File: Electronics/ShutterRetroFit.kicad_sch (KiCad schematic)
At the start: 20 parts, among them J1 AMPHENOL_12402012E212A, J2 AS5600, J3 Motor Terminals, Q1 SiSS52DN-T1-GE3, Q2 SiSS52DN-T1-GE3, Q3 SiSS52DN-T1-GE3, Q4 SiSS52DN-T1-GE3, U1 ESP32-WROOM-32, U2 CP2102N-Axx-xQFN28, U3 MIC4606-2YTS-TR, U4 AMS1117-3.3 (Potentially swap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, U5 LM2576S-ADJ

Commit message: Bulk sync with various changes made over the last year
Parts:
- removed F1, F2: Fuse, symbol Device:Fuse
- removed J2: AS5600, symbol Connector:Conn_01x04_Socket
- removed J3: Motor Terminals, symbol Connector:Conn_01x02_Pin
- removed Q1, Q2, Q3, Q4: SiSS52DN-T1-GE3, SISS94DNT1GE3, symbol CustomLibrary:SiSS52DN-T1-GE3
- removed R1: R_Shunt, symbol Device:R_Shunt
- removed RV1: R_Potentiometer_Trim, symbol Device:R_Potentiometer_Trim
- removed TH1, TH2, TH3, TH4: Thermistor, symbol Device:Thermistor
- removed U3: MIC4606-2YTS-TR, TSSOP16_TS_MCH_MIS, symbol CustomLibrary:MIC4606-2YTS-TR
- removed U4: AMS1117-3.3 (Potentially swap for a better LDO), Package_TO_SOT_SMD:SOT-223-3_TabPin2, symbol Regulator_Linear:AMS1117-3.3
- removed U5: LM2576S-ADJ, Package_TO_SOT_SMD:TO-263-5_TabPin3, symbol Regulator_Switching:LM2576S-ADJ
- added C1, C3, C5, C6, C7, C8: 0.1uF, Capacitor_SMD:C_0603_1608Metric_Pad1.08x0.95mm_HandSolder, symbol Device:C
- added C2: 1uF, Capacitor_SMD:C_0603_1608Metric_Pad1.08x0.95mm_HandSolder, symbol Device:C
- added C4: 22uF, Capacitor_SMD:C_0603_1608Metric_Pad1.08x0.95mm_HandSolder, symbol Device:C
- added H1, H2, H3, H4: MountingHole_Pad, MountingHole:MountingHole_3.2mm_M3_DIN965_Pad, symbol Mechanical:MountingHole_Pad
- added J2: AS5600, Connector_JST:JST_XH_B6B-XH-A_1x06_P2.50mm_Vertical, symbol Connector:Conn_01x06_Socket
- added J3: PWR_IN+, CustomLibrary:CONN_726386-2_TEC, symbol Connector:Conn_01x01_Pin
- added J4: EXP, Connector_PinHeader_2.54mm:PinHeader_1x06_P2.54mm_Vertical, symbol Connector:Conn_01x06_Pin
- added J5: CONTROL, Connector_JST:JST_XH_B6B-XH-A_1x06_P2.50mm_Vertical, symbol Connector:Conn_01x06_Socket
- added J6: PWR_IN-, CustomLibrary:CONN_726386-2_TEC, symbol Connector:Conn_01x01_Pin
- added R1, R2: 5k1, Resistor_SMD:R_0603_1608Metric_Pad0.98x0.95mm_HandSolder, symbol Device:R
- added R3, R4: 1k, Resistor_SMD:R_0603_1608Metric_Pad0.98x0.95mm_HandSolder, symbol Device:R
- added SW1: RESET, symbol Switch:SW_SPST
- added SW2: BOOT, symbol Switch:SW_SPST
- added TP1: RX, TestPoint:TestPoint_Pad_D1.0mm, symbol Connector:TestPoint
- added TP2: TX, TestPoint:TestPoint_Pad_D1.0mm, symbol Connector:TestPoint
- added TP3: IO0, TestPoint:TestPoint_Pad_D1.0mm, symbol Connector:TestPoint
- added TP4: EN, TestPoint:TestPoint_Pad_D1.0mm, symbol Connector:TestPoint
- U1: renamed from U2; value CP2102N-Axx-xQFN28 -> CP2102-Axx-xQFN28
- renumbered U1 to U2
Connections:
- net GND: now reaches J1.A1_B12 (GND)
- net GND: now also J1.B1_A12 (GND__1), J1.SH1 (SHIELD), J1.SH2 (SHIELD__1), J1.SH3 (SHIELD__2), J1.SH4 (SHIELD__3), U1.29 (GND), U1.3 (GND), U2.1 (GND), U2.15 (GND), U2.38 (GND), U2.39 (GND), C1.2, C2.2, C3.2, C4.2, C5.2, C6.2, C7.2, C8.2, H1.1, H2.1, H3.1, H4.1, J2.1 (Pin_1), J2.2 (Pin_2), J4.1 (Pin_1), J5.1 (Pin_1), J6.1 (Pin_1), R1.2, R2.2, SW1.2 (B), SW2.2 (B)
- net USB_{VBUS}: now reaches J1.A4_B9 (VBUS)
- net USB_{VBUS}: now also J1.B4_A9 (VBUS__1), U1.7 (VREGIN), U1.8 (VBUS), C2.1, C3.1
- net at J1.A5 (CC1_A): now also R1.1
- net DATA+: now reaches J1.A6 (D+_A)
- net DATA+: now also J1.B6 (D+_B), U1.4 (D+)
- net DATA-: now reaches J1.A7 (D-_A)
- net DATA-: now also J1.B7 (D-_B), U1.5 (D-)
- net at J1.B5 (CC1_B): now also R2.1
- net UART_{RX}: now reaches U1.25 (RXD)
- net UART_{RX}: now also U2.35 (TXD0/IO1), TP1.1
- net UART_{TX}: now reaches U1.26 (TXD)
- net UART_{TX}: now also U2.34 (RXD0/IO3), TP2.1
- net at U1.6 (VDD): now also C1.1
- net EXP_{02}: now reaches U2.10 (IO25)
- net EXP_{02}: now also J4.3 (Pin_3)
- net EXP_{01}: now reaches U2.11 (IO26)
- net EXP_{01}: now also J4.2 (Pin_2)
- net BTN_{UP}: now reaches U2.12 (IO27)
- net BTN_{UP}: now also C7.1, J5.3 (Pin_3), R3.1
- net H_{DRIVER_LEFT_EN}: now reaches U2.13 (IO14)
- net H_{DRIVER_LEFT_CONTROL}: now reaches U2.14 (IO12)
- net H_{DRIVER_RIGHT_EN}: now reaches U2.16 (IO13)
- net MCU_{VIN}: now reaches U2.2 (VDD)
- net MCU_{VIN}: now also C4.1
- net H_{DRIVER_RIGHT_CONTROL}: now reaches U2.23 (IO15)
- net IO0: now reaches U2.25 (IO0)
- net IO0: now also C5.1, SW1.1 (A), TP3.1
- net M_{SENSE}: now reaches U2.27 (IO16)
- net D_{POWER}: now reaches U2.28 (IO17)
- net D_{POWER}: now also J5.6 (Pin_6)
- net EN: now reaches U2.3 (EN)
- net EN: now also C6.1, SW2.1 (A), TP4.1
- net D_{STATUS}: now reaches U2.30 (IO18)
- net D_{STATUS}: now also J5.5 (Pin_5)
- net D_{ERROR}: now reaches U2.31 (IO19)
- net D_{ERROR}: now also J5.4 (Pin_4)
- net AS5600_{SDA}: now reaches U2.33 (IO21)
- net AS5600_{SDA}: now also J2.4 (Pin_4)
- net AS5600_{SCL}: now reaches U2.36 (IO22)
- net AS5600_{SCL}: now also J2.5 (Pin_5)
- net BTN_{DOWN}: now reaches U2.8 (IO32)
- net BTN_{DOWN}: now also C8.1, J5.2 (Pin_2), R4.1
- new net +12V: J3.1 (Pin_1)
- new net +12v_{EXP}: J4.6 (Pin_6)
- new net +3V3: R3.2, R4.2
- new net +3v3_{EXP}: J2.6 (Pin_6), J4.4 (Pin_4)
- new net +5v_{EXP}: J4.5 (Pin_5)
- no-connect marks 0 -> 1
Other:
- added sheet Motor (motor_sch.kicad_sch)
- added sheet Power Rails (PowerRails.kicad_sch)
- note added: "3.3v at Gate 12v at Source ~0v at Drain V_{gs} = 3.3v - 12v = ~ -8.7v V_{ds} = ~ -12v"
- note added: "Button pannel buttons should be pulling to ground"
- note added: "Do we want D+ and D- TPs?"
- note added: "V_{gs} > ~2v starts to conduct current To get optimal Rds_{on} then V_{gs} >= 6v Since these are low side mosfet, check what voltage they'd be recieving at the drain Theoretically this is fine as when conducting V_{gs} will be 3.3v and when not conducting stil 3.3v"
- company: (none) -> TowKnee
- title: (none) -> Shutter Motor Retro Fit
- moved on the sheet: J1, U1, U2

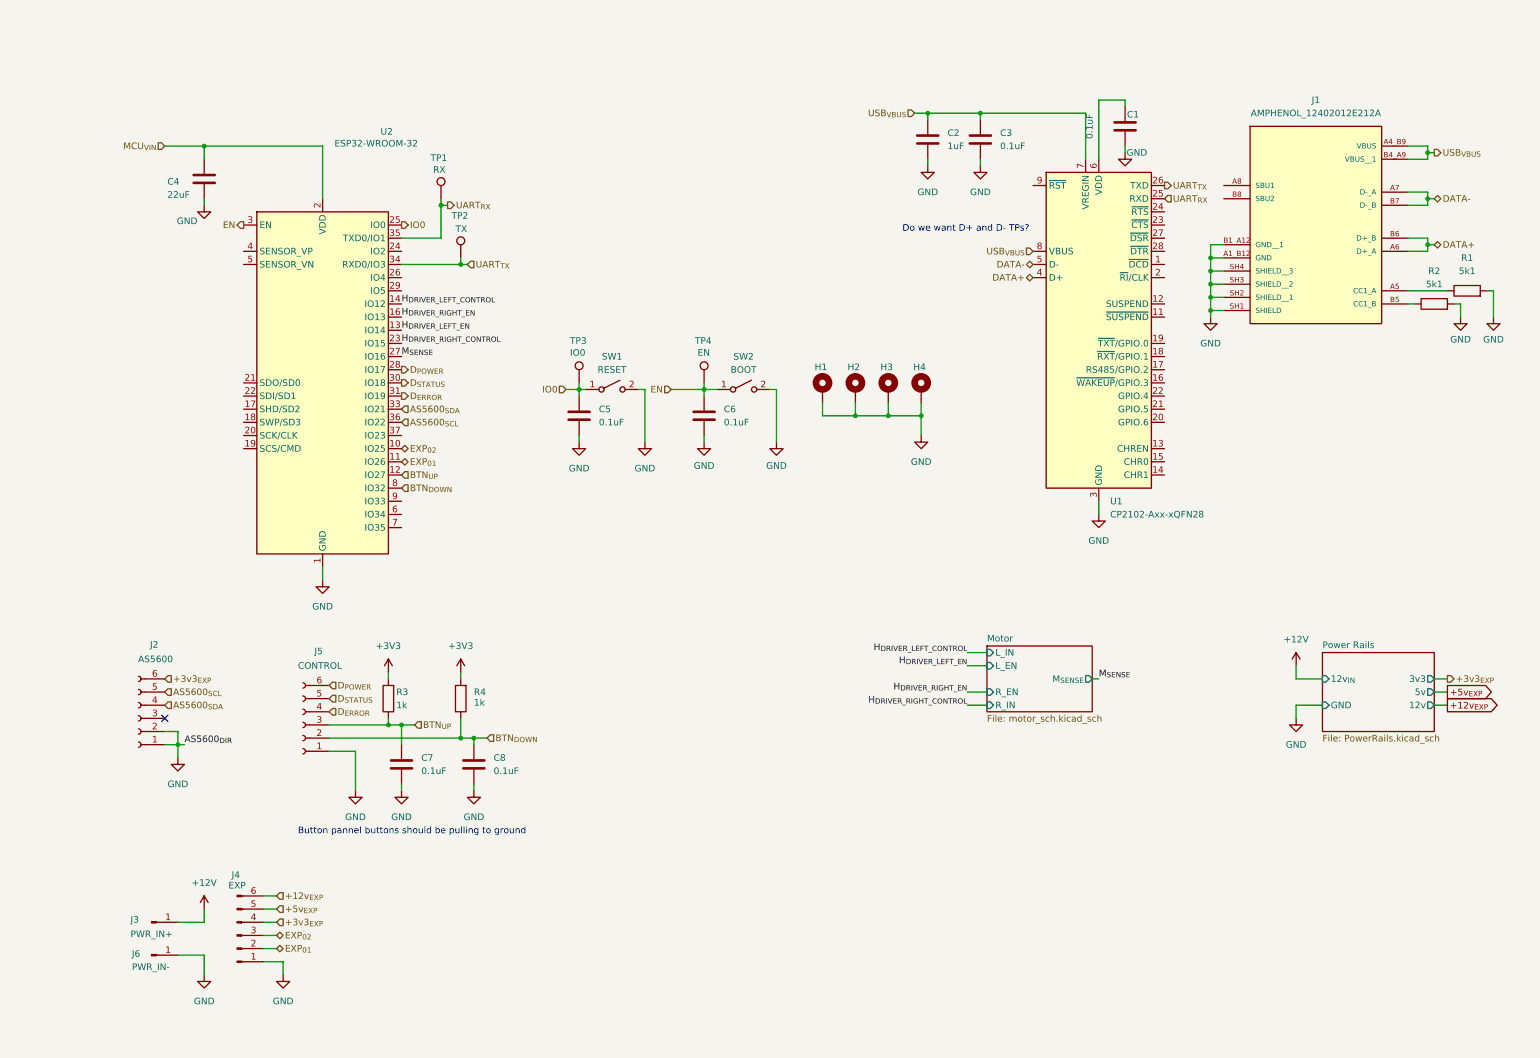
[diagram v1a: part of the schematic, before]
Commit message: Clean up schematic to be neater and repurposed AS5600 to be generic accessory connector
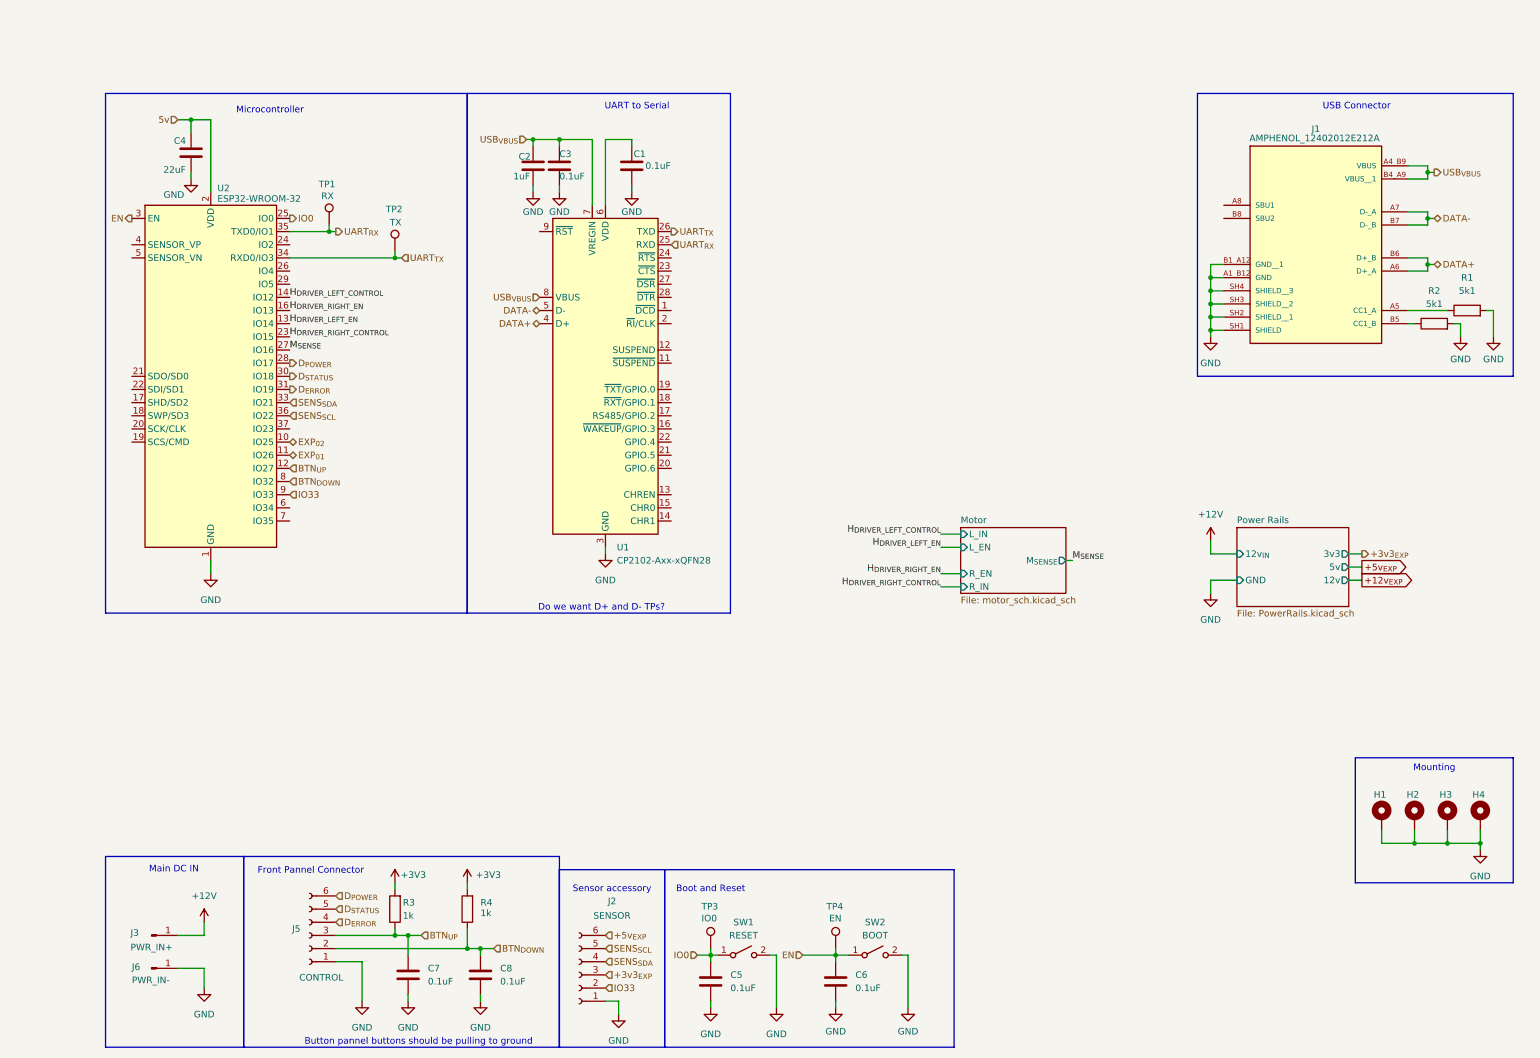
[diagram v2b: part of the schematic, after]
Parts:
- removed J4: EXP, Connector_PinHeader_2.54mm:PinHeader_1x06_P2.54mm_Vertical, symbol Connector:Conn_01x06_Pin
- J2: value AS5600 -> SENSOR
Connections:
- net +3v3_{EXP}: now also J2.3 (Pin_3); no longer J2.6 (Pin_6)
- net +5v_{EXP}: now also J2.6 (Pin_6)
- net GND: no longer J2.2 (Pin_2)
- net IO33: now reaches U2.9 (IO33)
- net IO33: now also J2.2 (Pin_2)
- net AS5600_{SCL} renamed SENS_{SCL}
- net AS5600_{SDA} renamed SENS_{SDA}
- net MCU_{VIN} renamed 5v
- no-connect marks 1 -> 0
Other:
- note added: "Boot and Reset"
- note added: "Front Pannel Connector"
- note added: "Main DC IN"
- note added: "Microcontroller"
- note added: "Mounting"
- note added: "Sensor accessory"
- note added: "UART to Serial"
- note added: "USB Connector"
- moved on the sheet: C1, C2, C3, C4, C5, C6, C7, C8, H1, H2, H3, H4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

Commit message: Electronics release 1.0
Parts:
- removed H4: MountingHole_Pad, MountingHole:MountingHole_3.2mm_M3_DIN965_Pad, symbol Mechanical:MountingHole_Pad
- removed J3: PWR_IN+, CustomLibrary:CONN_726386-2_TEC, symbol Connector:Conn_01x01_Pin
- removed J6: PWR_IN-, CustomLibrary:CONN_726386-2_TEC, symbol Connector:Conn_01x01_Pin
- added J3: PWR_IN+, symbol Connector:Conn_01x02_Pin
- added J6: PWR_IN-, symbol Connector:Conn_01x02_Pin
- C7, C8, R3, R4: now not fitted; now left out of the parts list
- J2: value SENSOR -> ACCESSORY
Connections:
- net EXP_{01} is gone; now on net H_{DRIVER_RIGHT_CONTROL}: U2.11 (IO26)
- net +12V: now also J3.1 (Pin_1), J3.2 (Pin_2)
- net BTN_{DOWN}: now also C7.1, J5.3 (Pin_3), R3.1; no longer C8.1, J5.2 (Pin_2), R4.1
- net BTN_{UP}: now also C8.1, J5.2 (Pin_2), R4.1; no longer C7.1, J5.3 (Pin_3), R3.1
- net D_{POWER}: now also U2.37 (IO23); no longer U2.28 (IO17)
- net GND: now also J6.1 (Pin_1), J6.2 (Pin_2)
- net H_{DRIVER_LEFT_CONTROL}: no longer U2.14 (IO12)
- net H_{DRIVER_RIGHT_CONTROL}: no longer U2.23 (IO15)
- net M_{SENSE}: now also U2.6 (IO34); no longer U2.27 (IO16)
- net SENS_{SCL}: now also J2.4 (Pin_4); no longer J2.5 (Pin_5)
- net SENS_{SDA}: now also J2.5 (Pin_5); no longer J2.4 (Pin_4)
- net +3v3_{EXP}: no longer names the net of J2.3 (Pin_3)
- net 5v renamed +3v3
- net EXP_{02}: no longer names the net of U2.10 (IO25)
- no-connect marks 0 -> 14
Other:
- note added: "Accessory"
- note added: "Add support for a foot pedal type external control instead of front panel buttons"
- note removed: "Sensor accessory"
